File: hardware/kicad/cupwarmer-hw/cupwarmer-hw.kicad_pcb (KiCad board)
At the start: 4 copper layers, 56 x 56 mm, 51 parts, among them J1 I2C Service, J3 STATUS_MON, Q1 AO3400 SOT-23, U1 STWLC38JRM

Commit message: Move F1 thermostat and TH2 NTC off-board
F1 (KSD9700 thermostat) and TH2 (heater NTC) are now part of the
heater assembly rather than the cupwarmer PCB; they ship together
with the JLCPCB silicone heater order. Drop F1's PCB footprint,
flip the schematic symbol to on_board=no, and add TH2 to the BOM
as an off-board NTC. Document R7=51k sizing for the OTP divider.

Co-Authored-By: Claude Opus 4.7 (1M context) <noreply@anthropic.com>
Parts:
- removed F1: KSD9700-70/5JSB/080C, Connector_Wire:SolderWire-0.5sqmm_1x02_P4.8mm_D0.9mm_OD2.3mm
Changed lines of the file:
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@@
-		)
-	)
-	(footprint "Connector_Wire:SolderWire-0.5sqmm_1x02_P4.8mm_D0.9mm_OD2.3mm"
-		(placed yes)
-		(layer "F.Cu")
-		(at 93 117.6 -90)
-		(descr "Soldered wire connection, for 2 times 0.5 mm² wires, reinforced insulation, conductor diameter 0.9mm, outer diameter 2.3mm, size source Multi-Contact FLEXI-xV 0.50 (https://www.staubli.com/content/dam/ecs/catalogs-brochures/TM/CAB-Main-11014119-en.pdf#page=11), bend radius 3 times outer diameter")
-		(tags "connector wire 0.5sqmm")
-		(property "Reference" "F1"
-			(at 2.4 2.5 90)
-			(layer "F.SilkS")
-			(effects
-				(font
-					(size 1 1)
-					(thickness 0.15)
-				)
-			)
-		)
-		(property "Value" "KSD9700-70/5JSB/080C"
-			(at 2.4 2.35 90)
-			(layer "F.Fab")
-			(effects
-				(font
-					(size 1 1)
-					(thickness 0.15)
-				)
-			)
-		)
-		(property "Datasheet" "~"
-			(at 0 0 90)
-			(layer "F.Fab")
-			(hide yes)
-			(effects
-				(font
-					(size 1.27 1.27)
-				)
-			)
-		)
-		(property "Description" "Independent thermal cutoff in series before heater"
-			(at 0 0 90)
-			(layer "F.Fab")
-			(hide yes)
-			(effects
-				(font
-					(size 1.27 1.27)
-				)
-			)
-		)
-		(property "KiLib_Generator" "connector/wire"
-			(at 0 0 90)
-			(layer "F.SilkS")
-			(hide yes)
-			(effects
-				(font
-					(size 1 1)
-					(thickness 0.15)
-				)
-			)
-		)
-		(property "Manufacturer" "Xucheng Elec"
-			(at 0 0 270)
-			(unlocked yes)
-			(layer "F.Fab")
-			(hide yes)
-			(effects
-				(font
-					(size 1 1)
-					(thickness 0.15)
-				)
-			)
-		)
-		(property "LCSC" "C156512"
-			(at 0 0 270)
-			(unlocked yes)
-			(layer "F.Fab")
-			(hide yes)
-			(effects
-				(font
-					(size 1 1)
-					(thickness 0.15)
-				)
-			)
-		)
-		(property "MPN" "KSD9700-70/5JSB/080C"
-			(at 0 0 270)
-			(unlocked yes)
-			(layer "F.Fab")
-			(hide yes)
-			(effects
-				(font
-					(size 1 1)
-					(thickness 0.15)
-				)
-			)
-		)
-		(sheetname "/heater-control/")
-		(sheetfile "heater-control.kicad_sch")
-		(units
-			(unit
-				(name "A")
-				(pins "1" "2")
-			)
-		)
-		(duplicate_pad_numbers_are_jumpers no)
-		(fp_rect
-			(start -1.9 -1.65)
-			(end 1.9 1.65)
-			(stroke
-				(width 0.05)
-				(type solid)
-			)
-			(fill no)
-			(layer "F.CrtYd")
-		)
-		(fp_rect
-			(start 2.9 -1.65)
-			(end 6.7 1.65)
-			(stroke
-				(width 0.05)
-				(type solid)
-			)
-			(fill no)
-			(layer "F.CrtYd")
-		)
-		(fp_circle
-			(center 0 0)
-			(end 1.15 0)
-			(stroke
-				(width 0.1)
-				(type solid)
-			)
-			(fill no)
-			(layer "F.Fab")
-		)
-		(fp_circle
-			(center 4.8 0)
-			(end 5.95 0)
-			(stroke
-				(width 0.1)
-				(type solid)
-			)
-			(fill no)
-			(layer "F.Fab")
-		)
-		(fp_text user "${REFERENCE}"
-			(at 2.4 0 0)
-			(layer "F.Fab")
-			(effects
-				(font
-					(size 0.82 0.82)
-					(thickness 0.12)
-				)
-			)
-		)
-		(pad "1" thru_hole roundrect
-			(at 0 0 270)
-			(size 2.3 2.3)
-			(drill 1.15)
-			(layers "*.Cu" "*.Mask")
-			(remove_unused_layers no)
-			(roundrect_rratio 0.108696)
-			(net "VOUT_12V")
-			(pinfunction "1_1")
-			(pintype "passive")
-		)
-		(pad "2" thru_hole circle
-			(at 4.8 0 270)
-			(size 2.3 2.3)
-			(drill 1.15)
-			(layers "*.Cu" "*.Mask")
-			(remove_unused_layers no)
-			(net "/heater-control/HEATER_IN")
-			(pinfunction "2_2")
-			(pintype "passive")
-		)
-		(embedded_fonts no)
-		(model "${KICAD10_3DMODEL_DIR}/Connector_Wire.3dshapes/SolderWire-0.5sqmm_1x02_P4.8mm_D0.9mm_OD2.3mm.step"
-			(offset
-				(xyz 0 0 0)
-			)
-			(scale
-				(xyz 1 1 1)
-			)
-			(rotate
-				(xyz 0 0 0)
-			)
 		)
 	)

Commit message: Lay out H1 heater harness as 1x4 inline connector
Redraw HEATER_HARNESS_4 symbol as a horizontal 1x4 with pins ordered
H+, NTC, NTC_GND, H- to match the heater harness physical lead
sequence for hand-soldering. Renumber pins (1=H+, 2=NTC, 3=NTC_GND,
4=H-) and rebuild the footprint as an inline 4-pad row at 5 mm pitch
with 1.4 mm holes for H+/H- and 1.0 mm holes for the NTC pair.
Schematic ERC clean; PCB H1 needs Update-from-Schematic to relink
nets and reposition.

Co-Authored-By: Claude Opus 4.7 (1M context) <noreply@anthropic.com>
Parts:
- moved H1 128.7 mm to (200.0, 200.0)
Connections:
- H1 pad 1: /heater-control/HEATER_IN -> (no net)
- H1 pad 2: /heater-control/HEATER_OUT -> (no net)
- H1 pad 3: RX_NTC -> (no net)
- H1 pad 4: SYS_GND -> (no net)
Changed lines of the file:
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@@
 		)
 	)
-	(footprint "cupwarmer:SolderWire-HeaterHarness_1x04_P5.0mm_D1.4mm"
-		(placed yes)
-		(layer "F.Cu")
-		(at 97.3 122.5)
-		(descr "Four-wire solder pads for silicone heater harness: H+, H-, NTC, NTC_GND, P5.0 mm")
-		(tags "connector wire heater harness ntc")
-		(property "Reference" "H1"
-			(at 2.5 -2.8 0)
-			(layer "F.SilkS")
-			(hide yes)
-			(effects
-				(font
-					(size 1 1)
-					(thickness 0.15)
-				)
-			)
-		)
-		(property "Value" "12R 12W Heater + 100k NTC"
-			(at 2.5 5.8 0)
-			(layer "F.Fab")
-			(effects
-				(font
-					(size 1 1)
-					(thickness 0.15)
-				)
-			)
-		)
-		(property "Datasheet" "~"
-			(at 0 0 0)
-			(layer "F.Fab")
-			(hide yes)
-			(effects
-				(font
-					(size 1.27 1.27)
-				)
-			)
-		)
-		(property "Description" "Four-wire silicone heater harness: H+ after F1, H- to Q1 drain, embedded 100k NTC to RX_NTC/SYS_GND"
-			(at 0 0 0)
-			(layer "F.Fab")
-			(hide yes)
-			(effects
-				(font
-					(size 1.27 1.27)
-				)
-			)
-		)
-		(property "KiLib_Generator" "manual"
-			(at 0 0 0)
-			(layer "F.SilkS")
-			(hide yes)
-			(effects
-				(font
-					(size 1 1)
-					(thickness 0.15)
-				)
-			)
-		)
-		(sheetname "/heater-control/")
-		(sheetfile "heater-control.kicad_sch")
-		(units
-			(unit
-				(name "A")
-				(pins "1" "2" "3" "4")
-			)
-		)
-		(duplicate_pad_numbers_are_jumpers no)
-		(fp_rect
-			(start -1.9 -1.9)
-			(end 6.9 4.9)
-			(stroke
-				(width 0.05)
-				(type solid)
-			)
-			(fill no)
-			(layer "F.CrtYd")
-		)
-		(fp_text user "${REFERENCE}"
-			(at 2.5 1.5 0)
-			(layer "F.Fab")
-			(effects
-				(font
-					(size 0.94 0.94)
-					(thickness 0.14)
-				)
-			)
-		)
-		(pad "1" thru_hole roundrect
-			(at 0 0)
-			(size 2.75 2.75)
-			(drill 1.4)
-			(layers "*.Cu" "*.Mask")
-			(remove_unused_layers no)
-			(roundrect_rratio 0.090909)
-			(net "/heater-control/HEATER_IN")
-			(pinfunction "1_1")
-			(pintype "passive")
-		)
-		(pad "2" thru_hole circle
-			(at 5 0)
-			(size 2.75 2.75)
-			(drill 1.4)
-			(layers "*.Cu" "*.Mask")
-			(remove_unused_layers no)
-			(net "/heater-control/HEATER_OUT")
-			(pinfunction "2_2")
-			(pintype "passive")
-		)
-		(pad "3" thru_hole circle
-			(at 0 3)
-			(size 2.2 2.2)
-			(drill 1)
-			(layers "*.Cu" "*.Mask")
-			(remove_unused_layers no)
-			(net "RX_NTC")
-			(pinfunction "NTC_3")
-			(pintype "passive")
-		)
-		(pad "4" thru_hole circle
-			(at 5 3)
-			(size 2.2 2.2)
-			(drill 1)
-			(layers "*.Cu" "*.Mask")
-			(remove_unused_layers no)
-			(net "SYS_GND")
-			(pinfunction "NTC_GND_4")
-			(pintype "passive")
-		)
-		(embedded_fonts no)
-	)
 	(footprint "Resistor_SMD:R_0805_2012Metric"
 		(placed yes)
@@
 	)
 	(embedded_fonts no)
+	(footprint "cupwarmer:SolderWire-HeaterHarness_1x04_P5.0mm_D1.4mm"
+		(layer "F.Cu")
+		(at 200 200 0)
+		(descr "Four-wire solder pads for silicone heater harness: H+, H-, NTC, NTC_GND")
+		(tags "connector wire heater harness ntc")
+		(property "Reference" "H1"
+			(at 7.5 -2.8 0)
+			(layer "F.SilkS")
+			(effects
+				(font
+					(size 1 1)
+					(thickness 0.15)
+				)
+			)
+		)
+		(property "Value" "12R 12W Heater + 100k NTC"
+			(at 7.5 2.8 0)
+			(layer "F.Fab")
+			(effects
+				(font
+					(size 1 1)
+					(thickness 0.15)
+				)
+			)
+		)
+		(property "KiLib_Generator" "manual"
+			(at 0 0 0)
+			(layer "F.SilkS")
+			(hide yes)
+			(effects
+				(font
+					(size 1 1)
+					(thickness 0.15)
+				)
+			)
+		)
+		(duplicate_pad_numbers_are_jumpers no)
+		(fp_rect
+			(start -1.9 -1.9)
+			(end 16.9 1.9)
+			(stroke
+				(width 0.05)
+				(type solid)
+			)
+			(fill no)
+			(layer "F.CrtYd")
+		)
+		(fp_text user "${REFERENCE}"
+			(at 7.5 -1.0 0)
+			(layer "F.Fab")
+			(effects
+				(font
+					(size 0.9 0.9)
+					(thickness 0.13)
+				)
+			)
+		)
+		(pad "1" thru_hole roundrect
+			(at 0 0)
+			(size 2.75 2.75)
+			(drill 1.4)
+			(layers "*.Cu" "*.Mask")
+			(remove_unused_layers no)
+			(roundrect_rratio 0.090909)
+		)
+		(pad "2" thru_hole circle
+			(at 15.0 0)
+			(size 2.75 2.75)
+			(drill 1.4)
+			(layers "*.Cu" "*.Mask")
+			(remove_unused_layers no)
+		)
+		(pad "3" thru_hole circle
+			(at 5.0 0)
+			(size 2.2 2.2)
+			(drill 1.0)
+			(layers "*.Cu" "*.Mask")
+			(remove_unused_layers no)
+		)
+		(pad "4" thru_hole circle
+			(at 10.0 0)
+			(size 2.2 2.2)
+			(drill 1.0)
+			(layers "*.Cu" "*.Mask")
+			(remove_unused_layers no)
+		)
+		(embedded_fonts no)
+	)
 )

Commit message: Mark H2 off-board; relabel H1/H2 as PCB-side / heater-side
Add H2 as the heater-side 4-pin connector, paired with H1 on the PCB
side. H2/F1/TH2/R_HTR remain visible on the schematic for
documentation of the heater assembly, but are excluded from the PCB
netlist via on_board=no.

Co-Authored-By: Claude Opus 4.7 (1M context) <noreply@anthropic.com>
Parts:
- renumbered H2 to H5
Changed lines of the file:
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@@
 		(descr "Mounting Hole 2.2mm, M2, no annular, generated by kicad-footprint-generator mountinghole.py")
 		(tags "mountinghole M2")
-		(property "Reference" "H2"
+		(property "Reference" "H5"
 			(at 0 -3.15 0)
 			(layer "F.SilkS")
@@
 		(embedded_fonts no)
 	)
+	(footprint "cupwarmer:SolderWire-HeaterHarness_1x04_P5.0mm_D1.4mm"
+		(layer "F.Cu")
+		(at 200 200)
+		(descr "Four-wire solder pads for silicone heater harness: H+, H-, NTC, NTC_GND")
+		(tags "connector wire heater harness ntc")
+		(property "Reference" "H1"
+			(at 7.5 -2.8 0)
+			(layer "F.SilkS")
+			(effects
+				(font
+					(size 1 1)
+					(thickness 0.15)
+				)
+			)
+		)
+		(property "Value" "12R 12W Heater + 100k NTC"
+			(at 7.5 2.8 0)
+			(layer "F.Fab")
+			(effects
+				(font
+					(size 1 1)
+					(thickness 0.15)
+				)
+			)
+		)
+		(property "Datasheet" ""
+			(at 0 0 0)
+			(layer "F.Fab")
+			(hide yes)
+			(effects
+				(font
+					(size 1.27 1.27)
+				)
+			)
+		)
+		(property "Description" ""
+			(at 0 0 0)
+			(layer "F.Fab")
+			(hide yes)
+			(effects
+				(font
+					(size 1.27 1.27)
+				)
+			)
+		)
+		(property "KiLib_Generator" "manual"
+			(at 0 0 0)
+			(layer "F.SilkS")
+			(hide yes)
+			(effects
+				(font
+					(size 1 1)
+					(thickness 0.15)
+				)
+			)
+		)
+		(duplicate_pad_numbers_are_jumpers no)
+		(fp_rect
+			(start -1.9 -1.9)
+			(end 16.9 1.9)
+			(stroke
+				(width 0.05)
+				(type solid)
+			)
+			(fill no)
+			(layer "F.CrtYd")
+		)
+		(fp_text user "${REFERENCE}"
+			(at 7.5 -1 0)
+			(layer "F.Fab")
+			(effects
+				(font
+					(size 0.9 0.9)
+					(thickness 0.13)
+				)
+			)
+		)
+		(pad "1" thru_hole roundrect
+			(at 0 0)
+			(size 2.75 2.75)
+			(drill 1.4)
+			(layers "*.Cu" "*.Mask")
+			(remove_unused_layers no)
+			(roundrect_rratio 0.090909)
+		)
+		(pad "2" thru_hole circle
+			(at 15 0)
+			(size 2.75 2.75)
+			(drill 1.4)
+			(layers "*.Cu" "*.Mask")
+			(remove_unused_layers no)
+		)
+		(pad "3" thru_hole circle
+			(at 5 0)
+			(size 2.2 2.2)
+			(drill 1)
+			(layers "*.Cu" "*.Mask")
+			(remove_unused_layers no)
+		)
+		(pad "4" thru_hole circle
+			(at 10 0)
+			(size 2.2 2.2)
+			(drill 1)
+			(layers "*.Cu" "*.Mask")
+			(remove_unused_layers no)
+		)
+		(embedded_fonts no)
+	)
 	(footprint "Capacitor_SMD:C_0603_1608Metric"
 		(placed yes)
@@
 	)
 	(embedded_fonts no)
-	(footprint "cupwarmer:SolderWire-HeaterHarness_1x04_P5.0mm_D1.4mm"
-		(layer "F.Cu")
-		(at 200 200 0)
-		(descr "Four-wire solder pads for silicone heater harness: H+, H-, NTC, NTC_GND")
-		(tags "connector wire heater harness ntc")
-		(property "Reference" "H1"
-			(at 7.5 -2.8 0)
-			(layer "F.SilkS")
-			(effects
-				(font
-					(size 1 1)
-					(thickness 0.15)
-				)
-			)
-		)
-		(property "Value" "12R 12W Heater + 100k NTC"
-			(at 7.5 2.8 0)
-			(layer "F.Fab")
-			(effects
-				(font
-					(size 1 1)
-					(thickness 0.15)
-				)
-			)
-		)
-		(property "KiLib_Generator" "manual"
-			(at 0 0 0)
-			(layer "F.SilkS")
-			(hide yes)
-			(effects
-				(font
-					(size 1 1)
-					(thickness 0.15)
-				)
-			)
-		)
-		(duplicate_pad_numbers_are_jumpers no)
-		(fp_rect
-			(start -1.9 -1.9)
-			(end 16.9 1.9)
-			(stroke
-				(width 0.05)
-				(type solid)
-			)
-			(fill no)
-			(layer "F.CrtYd")
-		)
-		(fp_text user "${REFERENCE}"
-			(at 7.5 -1.0 0)
-			(layer "F.Fab")
-			(effects
-				(font
-					(size 0.9 0.9)
-					(thickness 0.13)
-				)
-			)
-		)
-		(pad "1" thru_hole roundrect
-			(at 0 0)
-			(size 2.75 2.75)
-			(drill 1.4)
-			(layers "*.Cu" "*.Mask")
-			(remove_unused_layers no)
-			(roundrect_rratio 0.090909)
-		)
-		(pad "2" thru_hole circle
-			(at 15.0 0)
-			(size 2.75 2.75)
-			(drill 1.4)
-			(layers "*.Cu" "*.Mask")
-			(remove_unused_layers no)
-		)
-		(pad "3" thru_hole circle
-			(at 5.0 0)
-			(size 2.2 2.2)
-			(drill 1.0)
-			(layers "*.Cu" "*.Mask")
-			(remove_unused_layers no)
-		)
-		(pad "4" thru_hole circle
-			(at 10.0 0)
-			(size 2.2 2.2)
-			(drill 1.0)
-			(layers "*.Cu" "*.Mask")
-			(remove_unused_layers no)
-		)
-		(embedded_fonts no)
-	)
 )

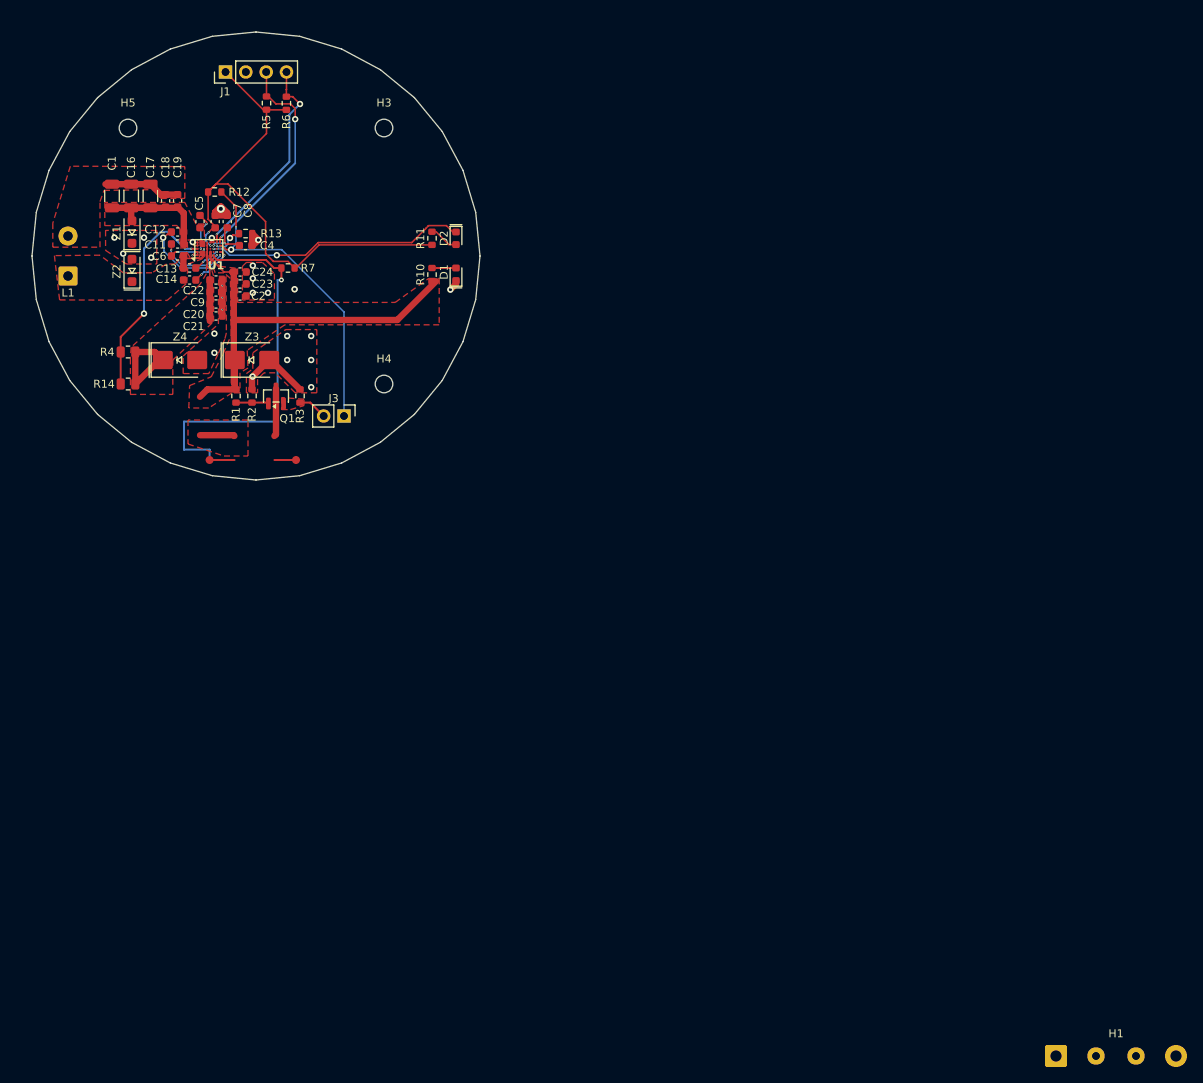
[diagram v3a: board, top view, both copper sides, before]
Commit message: Replace J3 bring-up header with TP3 test pad on I_HEATER_MON
Drop the dual-purpose 2-pin J3 (RX_INTB + I_HEATER_MON bring-up) and
expose only I_HEATER_MON via a single-pin TP3 test pad matching
TP1/TP2 (TESTPAD_1 symbol, 1x01 pin header footprint). RX_INTB stays
internal to the U1.H4 ↔ R12.1 path with its label moved onto that
net.

Co-Authored-By: Claude Opus 4.7 (1M context) <noreply@anthropic.com>
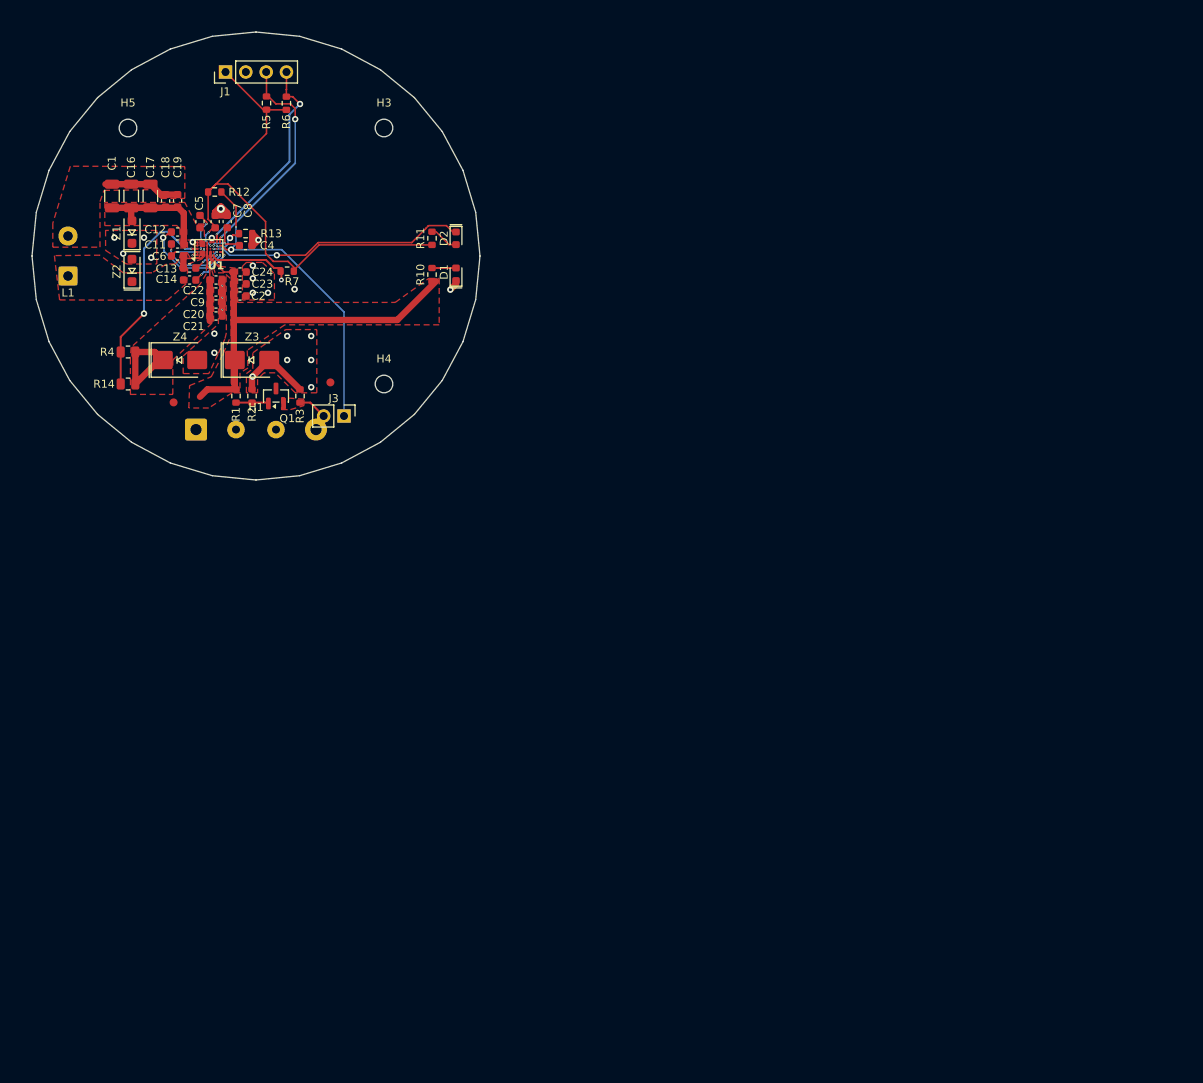
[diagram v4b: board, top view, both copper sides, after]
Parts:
- H1: value 12R 12W Heater + 100k NTC -> 4-pin heater lead pcb side
- moved H1 133.0 mm to (92.5, 121.7)
- moved TP2 10.6 mm to (109.3, 115.8)
- moved TP1 8.49 mm to (89.7, 118.3)
- moved R7 0.41 mm to (103.9, 101.9), turned to 180 degrees
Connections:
- H1 pad 1: (no net) -> VOUT_12V
- H1 pad 2: (no net) -> RX_NTC
- H1 pad 3: (no net) -> SYS_GND
- H1 pad 4: (no net) -> /heater-control/HEATER_OUT
- R7 pad 1: RX_NTC -> RX_VAA
- R7 pad 2: RX_VAA -> RX_NTC
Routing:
- net RX_NTC: track 54.8 -> 10.7 mm
- net /heater-control/HEATER_OUT: track 6.02 -> 0.00 mm
- net /heater-control/HEATER_IN: track 4.34 -> 0.00 mm
- net SYS_GND: track 34.3 -> 31.6 mm, vias 26 -> 25
- net RX_VAA: vias 2 -> 3
- removed copper zone on F.Cu, net /heater-control/HEATER_IN
